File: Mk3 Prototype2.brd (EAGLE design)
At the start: 119.6 x 68 mm, 143 parts, among them IC1 TPD3E001DRL, IC2 TPS62082, IC3 STM32F401V, IC4 BQ2409X, IC6 CC3100MOD, IC7 BQ2970, J1 ZX62-AB-5PA(11), J2 ER-TFT024-3, J3 SWD_SHROUD, Q1 DMMT5401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

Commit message: some prodding
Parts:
- added SG1: BUZZER-PKLCS1212E, TiLDA Mk3 Parts:BUZZER-PKLCS1212E
- moved FID3 29.0 mm to (8.50, 31.4)
- moved FID4 29.0 mm to (8.50, 31.4)
- moved S7 0.80 mm to (94.9, 53.4)
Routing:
- removed copper zone on layer 1, net GND

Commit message: cleaning up silk a little
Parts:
- removed SJ3: JUMPER-PAD-2-NOYES_SILK, SparkFun-Passives:PAD-JUMPER-2-NO_YES_SILK
- added R27: 0603/220k/5%, TiLDA Mk3 Parts:C0603K-SMALL
- added TP11: TPB1,27, TiLDA Mk3 Parts:B1,27
- moved U$2 1.60 mm to (35.2, 19.6)
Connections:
- new net N$17: IC6.10, R27.1, TP11.TP
- net GND: now also R27.2
- net USB_ID: no longer SJ3.1, SJ3.2
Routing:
- net TIM2_CH3: track 129.9 -> 140.8 mm
- net +3V3: track 437.7 -> 440.5 mm
- net TIM2_CH4: track 128.6 -> 130.3 mm
- net N$30: track 0.97 -> 0.00 mm
- net GND: vias 113 -> 111
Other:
- outline, holes or cut-outs redrawn
- board text added: "!CTS"
- board text added: "!RTS"
- board text added: "58"
- board text added: "59"
- board text added: "60"
- board text added: "62"
- board text removed: "*"
- board text removed: "OTG ID"

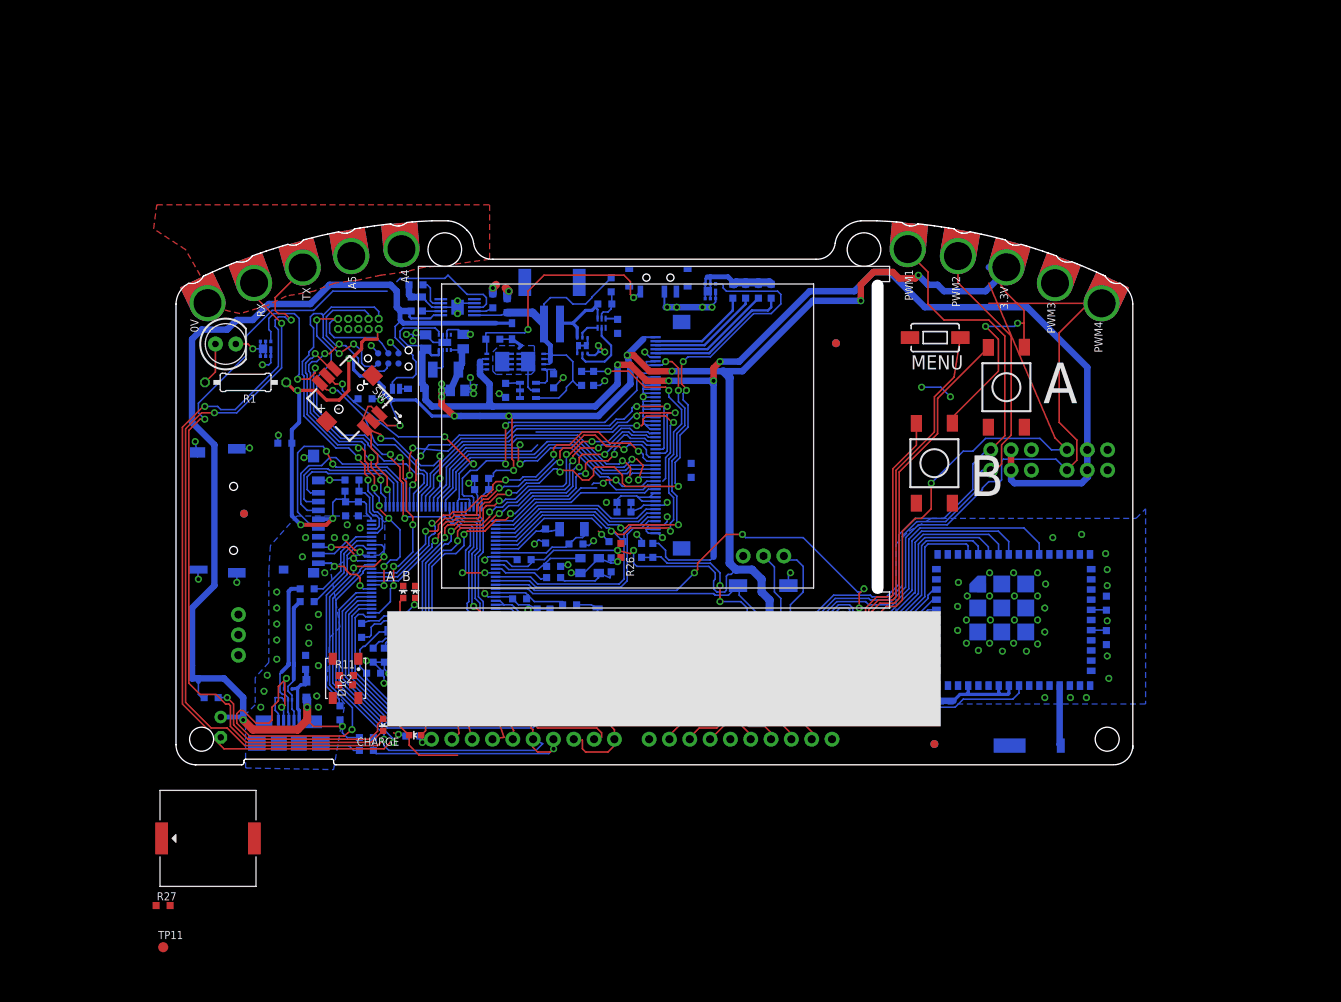
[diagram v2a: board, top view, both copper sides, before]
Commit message: mostly routed
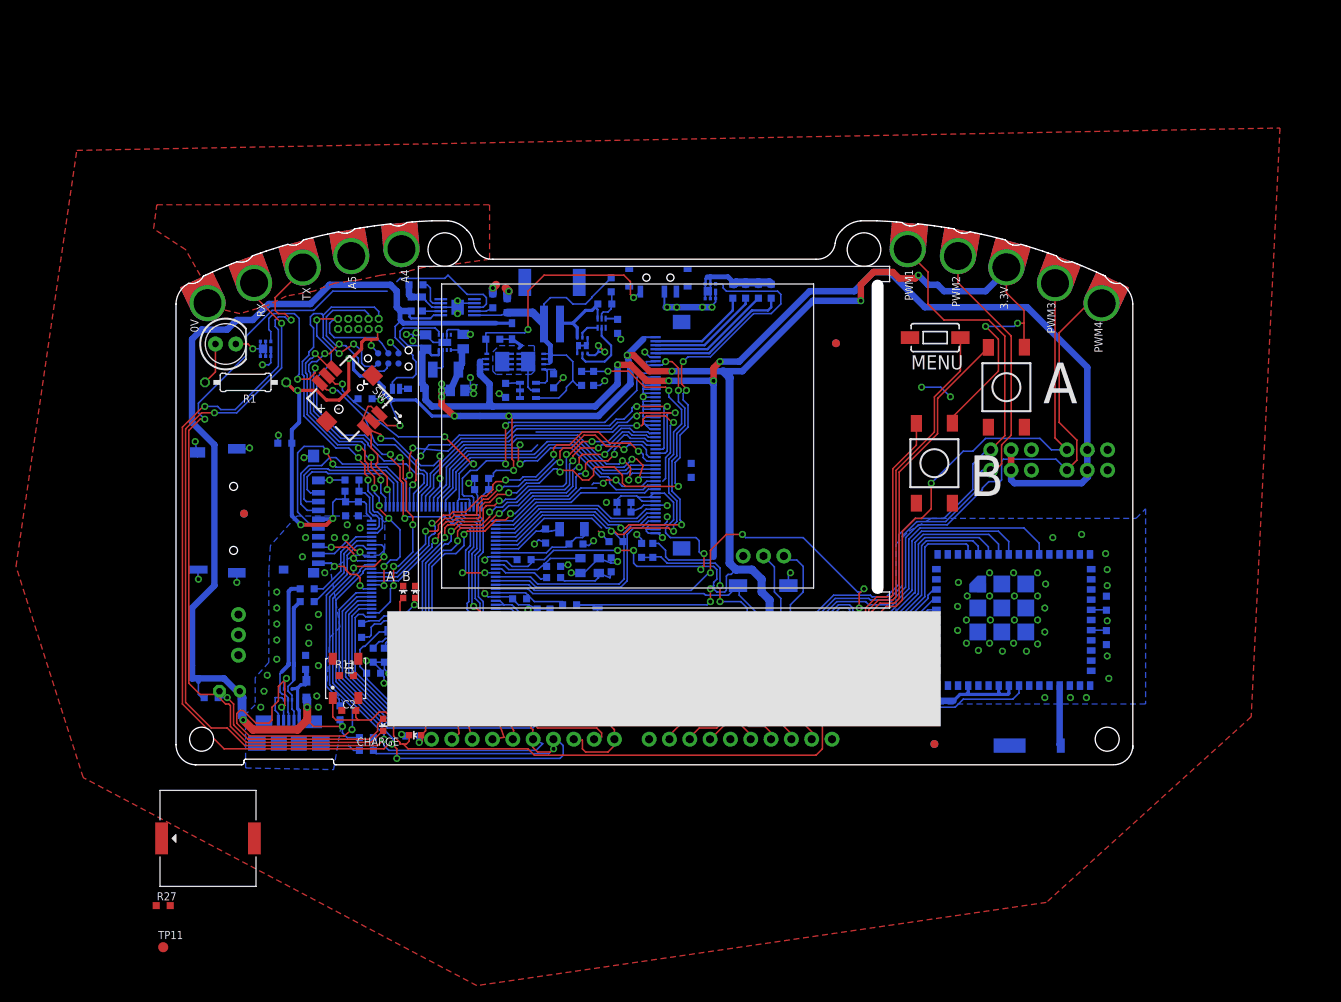
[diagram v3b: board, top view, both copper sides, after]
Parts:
- removed R26: TEmp, TiLDA Mk3 Parts:C0603K-SMALL
- moved C4 4.63 mm to (6.70, 9.20), turned to 0 degrees
- moved C2 3.22 mm to (21.6, 6.80)
- turned D1 to 90 degrees
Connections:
- net N$8: no longer R26.1
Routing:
- net +3V3: track 440.5 -> 541.0 mm, vias 24 -> 29
- net USART6_TX: track 123.8 -> 150.1 mm, vias 3 -> 4
- net TIM2_CH3: track 140.8 -> 129.9 mm
- net TIM2_CH4: track 130.3 -> 129.1 mm
- net CC_IRQ: track 88.0 -> 89.1 mm
- net VBUS: track 147.1 -> 147.9 mm
- net LCD_MODE: track 53.9 -> 54.4 mm
- net GND: track 187.3 -> 187.4 mm, vias 111 -> 112
- added copper zone on layer 1, net GND

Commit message: 6 airwires remain
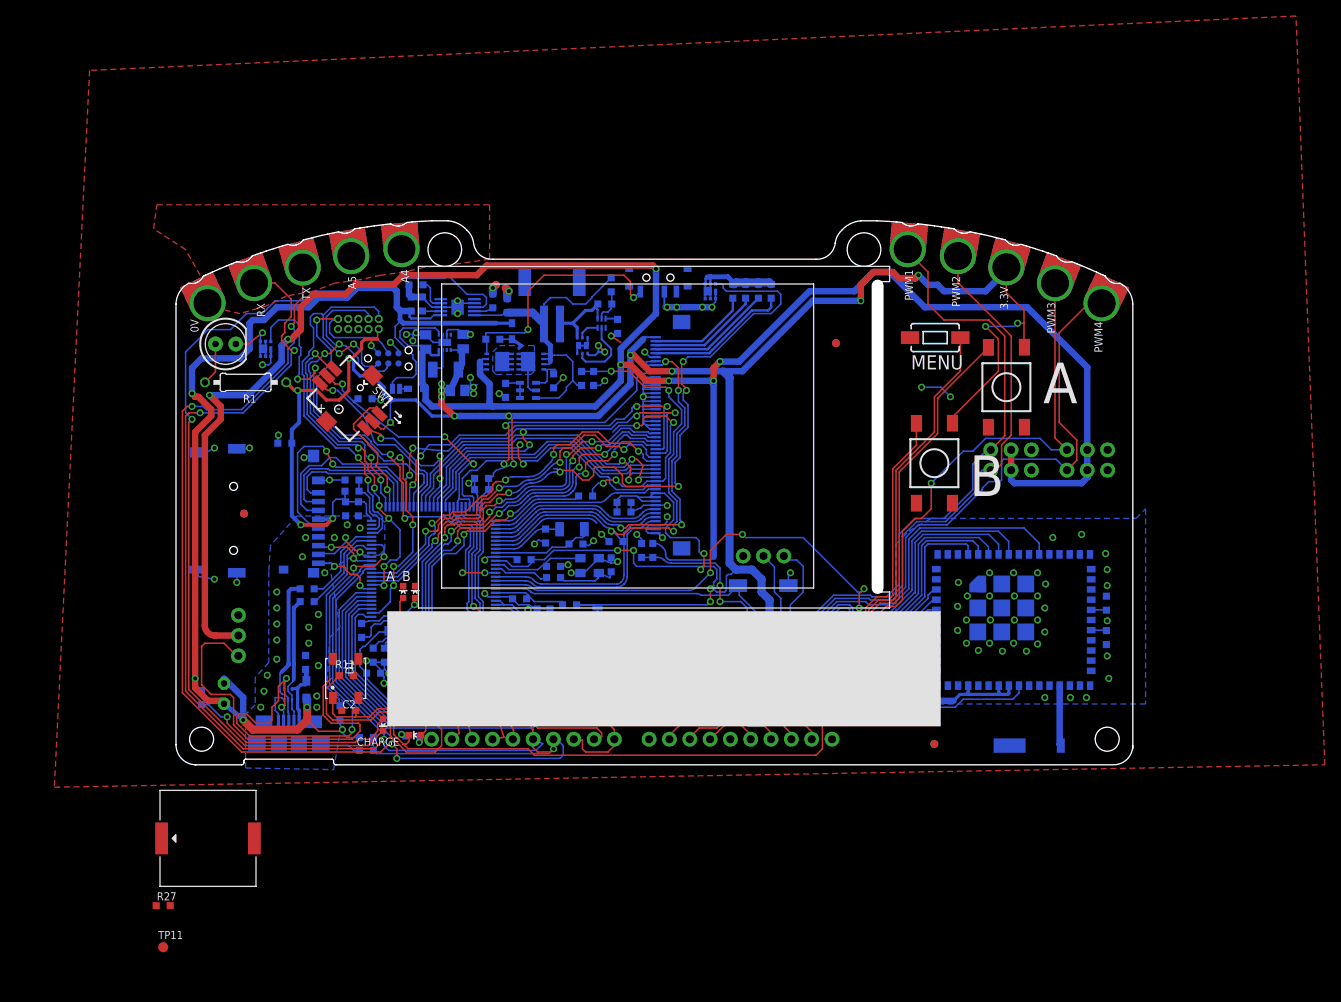
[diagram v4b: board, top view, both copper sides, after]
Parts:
- moved R24 13.6 mm to (51.2, 33.6), turned to 0 degrees
- moved SV2 5.00 mm to (7.80, 18.7), turned to 270 degrees
- moved R2 1.20 mm to (3.20, 8.40), turned to 90 degrees
- moved C4 0.76 mm to (6.00, 8.90), turned to 90 degrees
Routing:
- net V_UNREG: track 187.2 -> 301.0 mm, vias 4 -> 7
- net N$21: track 0.00 -> 46.2 mm
- net BOOT1: track 65.3 -> 98.4 mm, vias 0 -> 1
- net SPI3_SCK: track 53.0 -> 46.4 mm, vias 4 -> 6
- net USART6_RX: track 138.3 -> 143.3 mm
- net +3V3: track 541.0 -> 536.3 mm
- net N$9: track 112.0 -> 115.9 mm
- net GND: track 187.4 -> 190.5 mm, vias 112 -> 117
- net USART6_TX: track 150.1 -> 147.1 mm
- net FSMC_A23: track 14.3 -> 11.5 mm
- net TIM1_CH1N: track 60.6 -> 58.6 mm
- net USART1_TX: track 107.4 -> 105.9 mm
- net N$14: track 7.88 -> 9.22 mm
- net N$8: track 15.1 -> 14.0 mm
- net VBUS: track 147.9 -> 146.8 mm, vias 3 -> 5
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
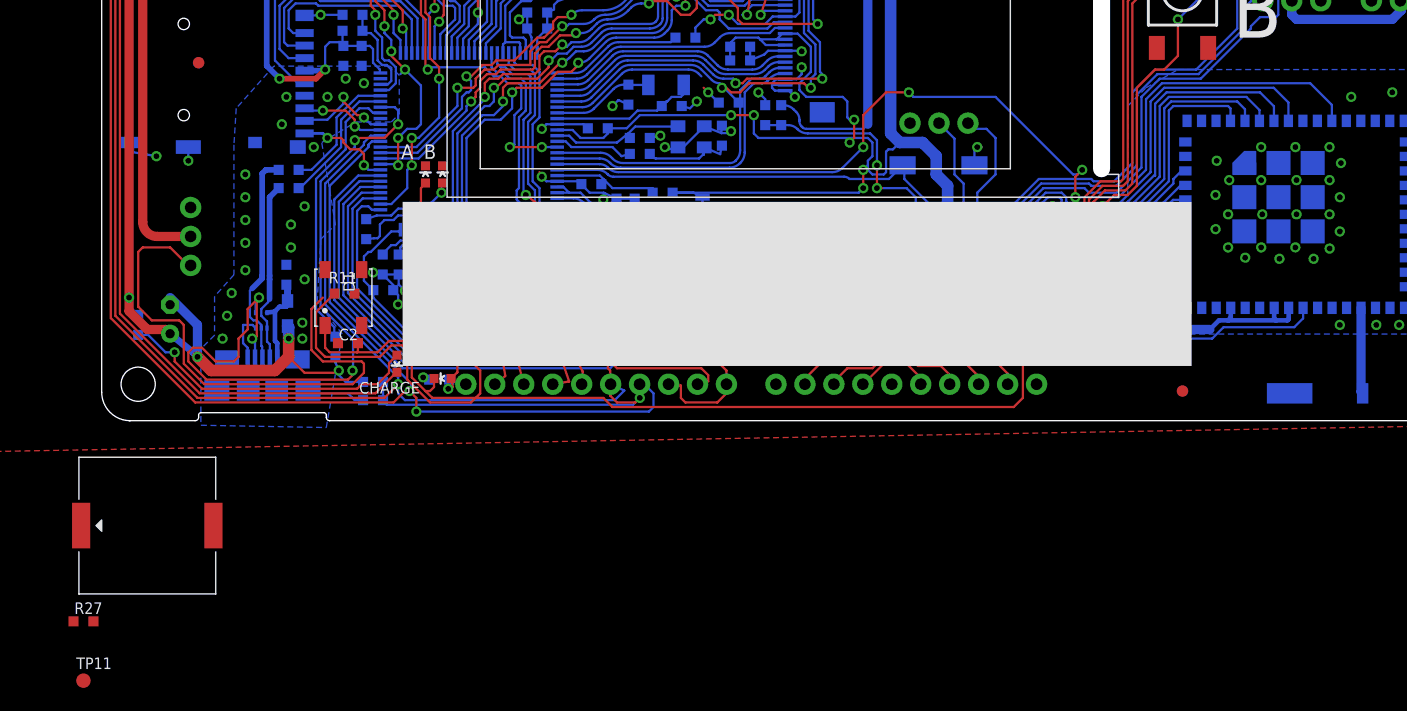
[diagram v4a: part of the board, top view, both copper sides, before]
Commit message: added pulldown to board
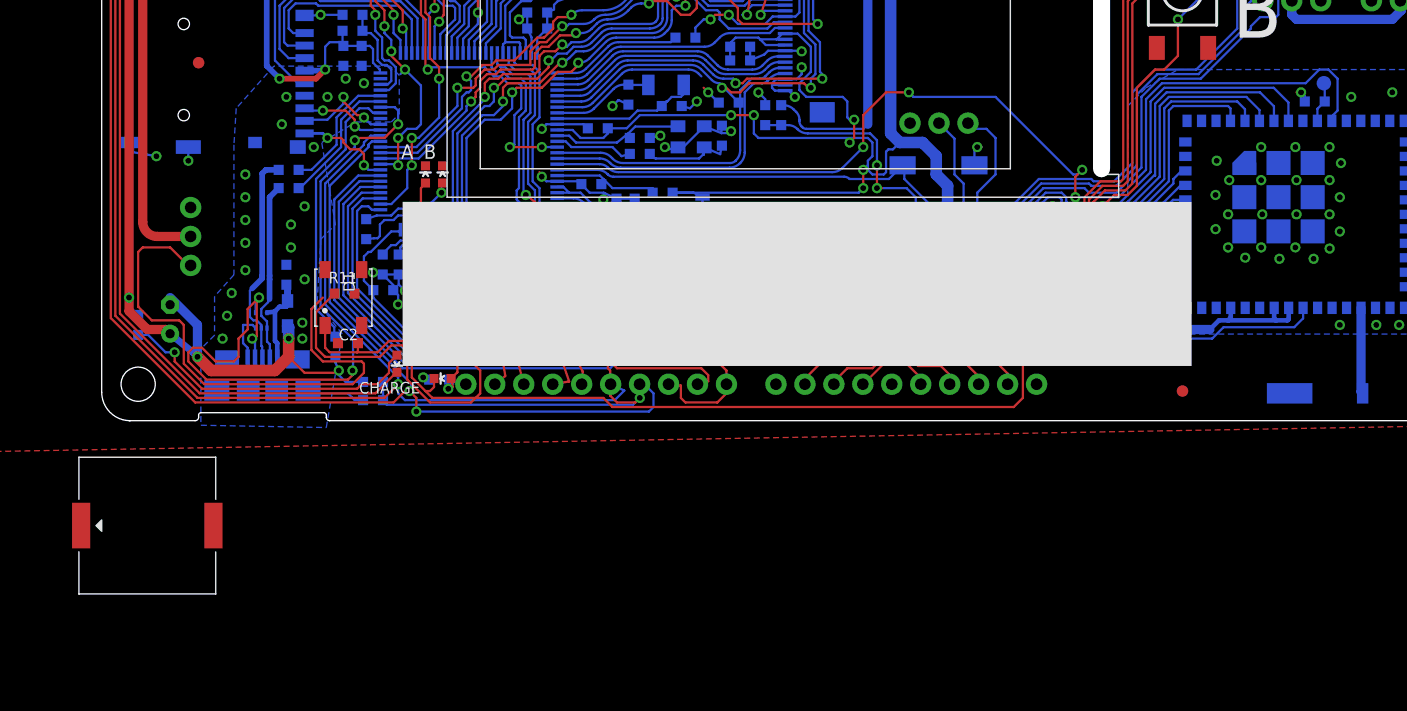
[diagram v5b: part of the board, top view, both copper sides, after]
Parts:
- moved TP11 120.8 mm to (107.2, 29.6), flipped to the bottom
- moved R27 117.2 mm to (106.4, 28.0), flipped to the bottom
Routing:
- net N$17: track 0.00 -> 3.60 mm
- net CC_IRQ: track 89.1 -> 92.2 mm
- net GND: track 190.5 -> 191.8 mm, vias 117 -> 118
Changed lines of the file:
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@@
 </element>
 <element name="SG1" library="TiLDA Mk3 Parts" package="BUZZER-PKLCS1212E" value="BUZZER-PKLCS1212E" x="4" y="-9.2" smashed="yes"/>
-<element name="R27" library="TiLDA Mk3 Parts" package="C0603K-SMALL" value="0603/220k/5%" x="-1.6" y="-17.6" smashed="yes">
-<attribute name="NAME" x="-2.4" y="-16.95" size="1.016" layer="25" font="vector" ratio="14"/>
+<element name="R27" library="TiLDA Mk3 Parts" package="C0603K-SMALL" value="0603/220k/5%" x="106.4" y="28" smashed="yes" rot="MR0">
+<attribute name="NAME" x="104.8" y="27.85" size="1.016" layer="26" font="vector" ratio="14" rot="MR0"/>
 </element>
-<element name="TP11" library="TiLDA Mk3 Parts" package="B1,27" value="TPB1,27" x="-1.6" y="-22.8" smashed="yes">
-<attribute name="TP_SIGNAL_NAME" value="" x="-2.235" y="-24.705" size="1" layer="37"/>
-<attribute name="NAME" x="-2.235" y="-21.784" size="1.016" layer="25" font="vector" ratio="14"/>
-<attribute name="VALUE" x="-2.235" y="-23.562" size="1.016" layer="27" font="vector" ratio="14"/>
+<element name="TP11" library="TiLDA Mk3 Parts" package="B1,27" value="TPB1,27" x="107.2" y="29.6" smashed="yes" rot="MR0">
+<attribute name="TP_SIGNAL_NAME" value="" x="107.835" y="27.695" size="1" layer="38" rot="MR0"/>
+<attribute name="VALUE" x="107.835" y="28.838" size="1.016" layer="28" font="vector" ratio="14" rot="MR0"/>
 </element>
 </elements>
@@
 <via x="97.7" y="19.8" extent="1-16" drill="0.5" shape="octagon"/>
 <via x="97.8" y="22.8" extent="1-16" drill="0.5" shape="octagon"/>
-<wire x1="10.1" y1="2.7" x2="-0.725" y2="-17.6" width="0" layer="19" extent="1-16"/>
+<wire x1="105.525" y1="28" x2="105.525" y2="28.475" width="0.2" layer="16"/>
+<wire x1="105.525" y1="28.475" x2="105.2" y2="28.8" width="0.2" layer="16"/>
+<via x="105.2" y="28.8" extent="1-16" drill="0.5" shape="octagon"/>
+<wire x1="105.2" y1="28.8" x2="104.8" y2="28.8" width="0.2" layer="1"/>
 </signal>
 <signal name="LCD_!RST">
@@
 <contactref element="IC6" pad="11"/>
 <contactref element="IC3" pad="17"/>
-<wire x1="107.9" y1="26.3" x2="107.9" y2="27.7" width="0.2" layer="16"/>
-<wire x1="107.9" y1="27.7" x2="106" y2="29.6" width="0.2" layer="16"/>
-<wire x1="106" y1="29.6" x2="93" y2="29.6" width="0.2" layer="16"/>
 <wire x1="93" y1="29.6" x2="91.6" y2="28.2" width="0.2" layer="16"/>
 <wire x1="91.6" y1="28.2" x2="91.6" y2="22" width="0.2" layer="16"/>
@@
 <wire x1="64.07395" y1="21.8" x2="64.971975" y2="22.171975" width="0.2" layer="16" curve="45"/>
 <wire x1="64.971975" y1="22.171975" x2="66.8" y2="24" width="0.2" layer="16"/>
+<wire x1="93" y1="29.6" x2="105.6" y2="29.6" width="0.2" layer="16"/>
+<wire x1="105.6" y1="29.6" x2="106.8" y2="30.8" width="0.2" layer="16"/>
+<wire x1="106.8" y1="30.8" x2="107.6" y2="30.8" width="0.2" layer="16"/>
+<wire x1="107.6" y1="30.8" x2="108.4" y2="30" width="0.2" layer="16"/>
+<wire x1="108.4" y1="30" x2="108.4" y2="27.2" width="0.2" layer="16"/>
+<wire x1="108.4" y1="27.2" x2="108" y2="26.8" width="0.2" layer="16"/>
+<wire x1="108" y1="26.8" x2="108" y2="26.4" width="0.2" layer="16"/>
+<wire x1="108" y1="26.4" x2="107.9" y2="26.3" width="0.2" layer="16"/>
 </signal>
 <signal name="USART1_RX">
@@
 <contactref element="R27" pad="1"/>
 <contactref element="TP11" pad="TP"/>
-<wire x1="-2.475" y1="-17.6" x2="106.63" y2="26.3" width="0" layer="19" extent="1-16"/>
-<wire x1="-1.6" y1="-22.8" x2="-2.475" y2="-17.6" width="0" layer="19" extent="1-1"/>
+<wire x1="106.63" y1="26.3" x2="106.63" y2="27.355" width="0.2" layer="16"/>
+<wire x1="106.63" y1="27.355" x2="107.275" y2="28" width="0.2" layer="16"/>
+<wire x1="107.275" y1="28" x2="107.275" y2="29.525" width="0.2" layer="16"/>
+<wire x1="107.275" y1="29.525" x2="107.2" y2="29.6" width="0.2" layer="16"/>
 </signal>
 </signals>
